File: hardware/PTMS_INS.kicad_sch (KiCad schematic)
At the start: 0 parts

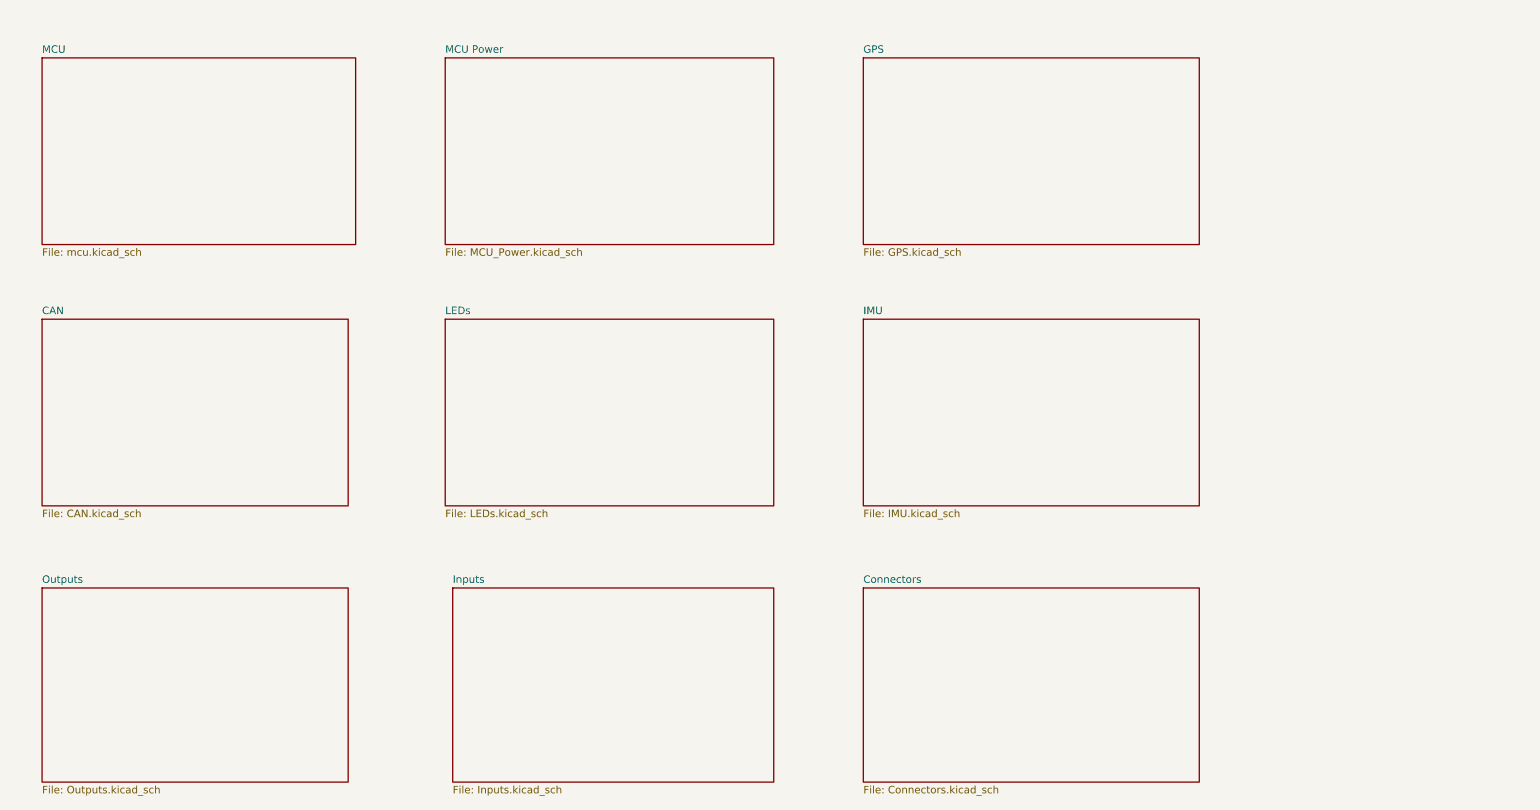
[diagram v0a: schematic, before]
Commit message: wire up altimeter, temp, barometer, imu, gps to MCU
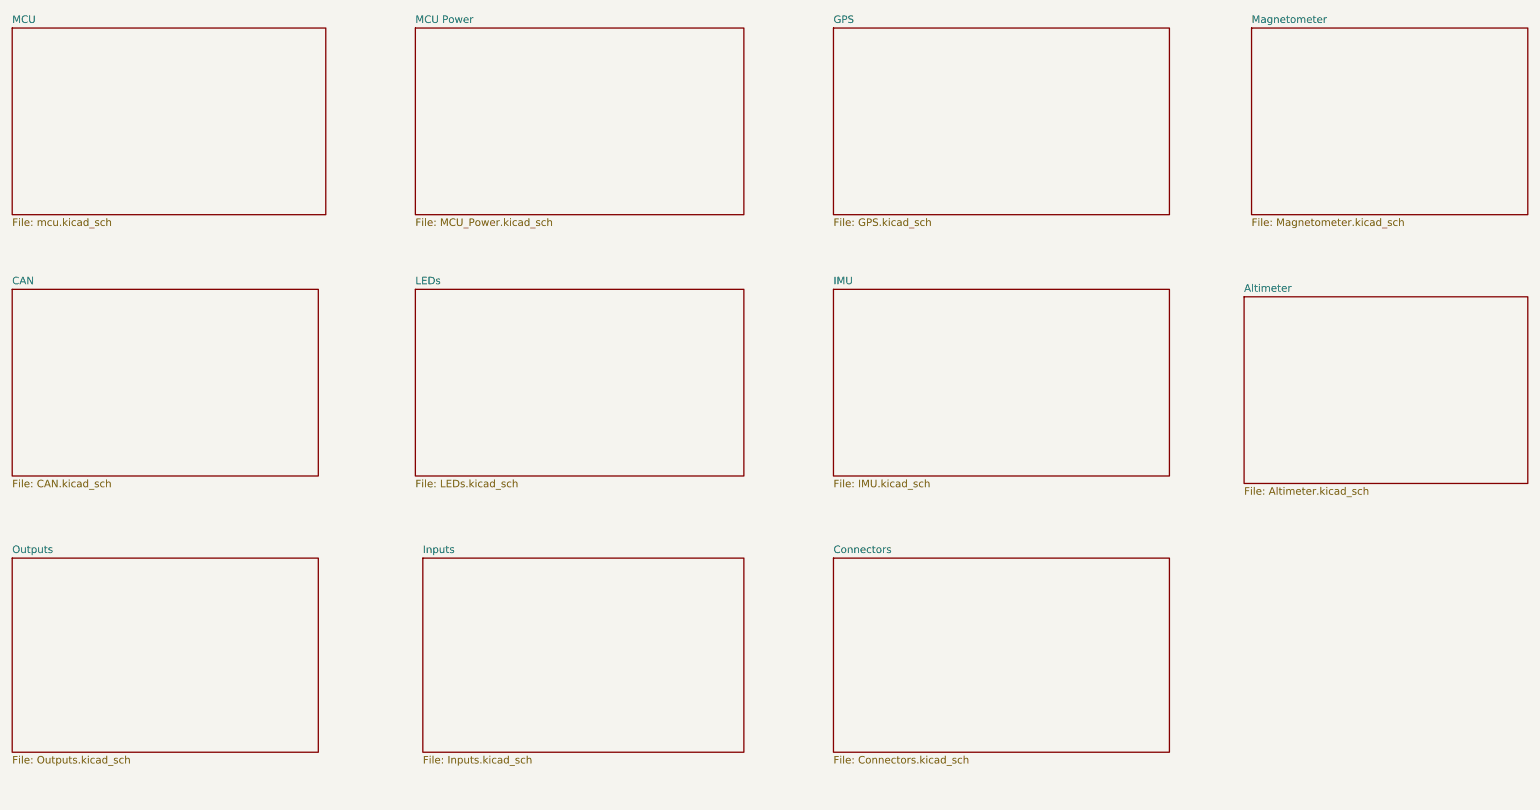
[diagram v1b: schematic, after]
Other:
- added sheet Altimeter (Altimeter.kicad_sch)
- added sheet Magnetometer (Magnetometer.kicad_sch)
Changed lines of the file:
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@@
 	(paper "A4")
 	(sheet
-		(at 25.4 123.19)
+		(at 20.32 118.11)
 		(size 52.07 33.02)
 		(exclude_from_sim no)
@@
 		)
 		(property "Sheetname" "Outputs"
-			(at 25.4 122.4784 0)
+			(at 20.32 117.3984 0)
 			(show_name no)
 			(do_not_autoplace no)
@@
 		)
 		(property "Sheetfile" "Outputs.kicad_sch"
-			(at 25.4 156.7946 0)
+			(at 20.32 151.7146 0)
 			(show_name no)
 			(do_not_autoplace no)
@@
 	)
 	(sheet
-		(at 165.1 77.47)
+		(at 160.02 72.39)
 		(size 57.15 31.75)
 		(exclude_from_sim no)
@@
 		)
 		(property "Sheetname" "IMU"
-			(at 165.1 76.7584 0)
+			(at 160.02 71.6784 0)
 			(show_name no)
 			(do_not_autoplace no)
@@
 		)
 		(property "Sheetfile" "IMU.kicad_sch"
-			(at 165.1 109.8046 0)
+			(at 160.02 104.7246 0)
 			(show_name no)
 			(do_not_autoplace no)
@@
 	)
 	(sheet
-		(at 95.25 123.19)
+		(at 90.17 118.11)
 		(size 54.61 33.02)
 		(exclude_from_sim no)
@@
 		)
 		(property "Sheetname" "Inputs"
-			(at 95.25 122.4784 0)
+			(at 90.17 117.3984 0)
 			(show_name no)
 			(do_not_autoplace no)
@@
 		)
 		(property "Sheetfile" "Inputs.kicad_sch"
-			(at 95.25 156.7946 0)
+			(at 90.17 151.7146 0)
 			(show_name no)
 			(do_not_autoplace no)
@@
 	)
 	(sheet
-		(at 93.98 77.47)
+		(at 229.87 73.66)
+		(size 48.26 31.75)
+		(exclude_from_sim no)
+		(in_bom yes)
+		(on_board yes)
+		(dnp no)
+		(fields_autoplaced yes)
+		(stroke
+			(width 0.1524)
+			(type solid)
+		)
+		(fill
+			(color 0 0 0 0)
+		)
+		(property "Sheetname" "Altimeter"
+			(at 229.87 72.9484 0)
+			(show_name no)
+			(do_not_autoplace no)
+			(effects
+				(font
+					(size 1.27 1.27)
+				)
+				(justify left bottom)
+			)
+		)
+		(property "Sheetfile" "Altimeter.kicad_sch"
+			(at 229.87 105.9946 0)
+			(show_name no)
+			(do_not_autoplace no)
+			(effects
+				(font
+					(size 1.27 1.27)
+				)
+				(justify left top)
+			)
+		)
+		(instances
+			(project "PTMS_INS"
+				(path "/7abec38e-2a6a-4c7d-a187-5990bacce22b"
+					(page "12")
+				)
+			)
+		)
+	)
+	(sheet
+		(at 88.9 72.39)
 		(size 55.88 31.75)
 		(exclude_from_sim no)
@@
 		)
 		(property "Sheetname" "LEDs"
-			(at 93.98 76.7584 0)
+			(at 88.9 71.6784 0)
 			(show_name no)
 			(do_not_autoplace no)
@@
 		)
 		(property "Sheetfile" "LEDs.kicad_sch"
-			(at 93.98 109.8046 0)
+			(at 88.9 104.7246 0)
 			(show_name no)
 			(do_not_autoplace no)
@@
 	)
 	(sheet
-		(at 25.4 33.02)
+		(at 20.32 27.94)
 		(size 53.34 31.75)
 		(exclude_from_sim no)
@@
 		)
 		(property "Sheetname" "MCU"
-			(at 25.4 32.3084 0)
+			(at 20.32 27.2284 0)
 			(show_name no)
 			(do_not_autoplace no)
@@
 		)
 		(property "Sheetfile" "mcu.kicad_sch"
-			(at 25.4 65.3546 0)
+			(at 20.32 60.2746 0)
 			(show_name no)
 			(do_not_autoplace no)
@@
 	)
 	(sheet
-		(at 165.1 123.19)
+		(at 160.02 118.11)
 		(size 57.15 33.02)
 		(exclude_from_sim no)
@@
 		)
 		(property "Sheetname" "Connectors"
-			(at 165.1 122.4784 0)
+			(at 160.02 117.3984 0)
 			(show_name no)
 			(do_not_autoplace no)
@@
 		)
 		(property "Sheetfile" "Connectors.kicad_sch"
-			(at 165.1 156.7946 0)
+			(at 160.02 151.7146 0)
 			(show_name no)
 			(do_not_autoplace no)
@@
 	)
 	(sheet
-		(at 93.98 33.02)
+		(at 231.14 27.94)
+		(size 46.99 31.75)
+		(exclude_from_sim no)
+		(in_bom yes)
+		(on_board yes)
+		(dnp no)
+		(fields_autoplaced yes)
+		(stroke
+			(width 0.1524)
+			(type solid)
+		)
+		(fill
+			(color 0 0 0 0)
+		)
+		(property "Sheetname" "Magnetometer"
+			(at 231.14 27.2284 0)
+			(show_name no)
+			(do_not_autoplace no)
+			(effects
+				(font
+					(size 1.27 1.27)
+				)
+				(justify left bottom)
+			)
+		)
+		(property "Sheetfile" "Magnetometer.kicad_sch"
+			(at 231.14 60.2746 0)
+			(show_name no)
+			(do_not_autoplace no)
+			(effects
+				(font
+					(size 1.27 1.27)
+				)
+				(justify left top)
+			)
+		)
+		(property "Field2" ""
+			(at 231.14 27.94 0)
+			(hide yes)
+			(show_name no)
+			(do_not_autoplace no)
+			(effects
+				(font
+					(size 1.27 1.27)
+				)
+			)
+		)
+		(instances
+			(project "PTMS_INS"
+				(path "/7abec38e-2a6a-4c7d-a187-5990bacce22b"
+					(page "11")
+				)
+			)
+		)
+	)
+	(sheet
+		(at 88.9 27.94)
 		(size 55.88 31.75)
 		(exclude_from_sim no)
@@
 		)
 		(property "Sheetname" "MCU Power"
-			(at 93.98 32.3084 0)
+			(at 88.9 27.2284 0)
 			(show_name no)
 			(do_not_autoplace no)
@@
 		)
 		(property "Sheetfile" "MCU_Power.kicad_sch"
-			(at 93.98 65.3546 0)
+			(at 88.9 60.2746 0)
 			(show_name no)
 			(do_not_autoplace no)
@@
 	)
 	(sheet
-		(at 25.4 77.47)
+		(at 20.32 72.39)
 		(size 52.07 31.75)
 		(exclude_from_sim no)
@@
 		)
 		(property "Sheetname" "CAN"
-			(at 25.4 76.7584 0)
+			(at 20.32 71.6784 0)
 			(show_name no)
 			(do_not_autoplace no)
@@
 		)
 		(property "Sheetfile" "CAN.kicad_sch"
-			(at 25.4 109.8046 0)
+			(at 20.32 104.7246 0)
 			(show_name no)
 			(do_not_autoplace no)
@@
 	)
 	(sheet
-		(at 165.1 33.02)
+		(at 160.02 27.94)
 		(size 57.15 31.75)
 		(exclude_from_sim no)
@@
 		)
 		(property "Sheetname" "GPS"
-			(at 165.1 32.3084 0)
+			(at 160.02 27.2284 0)
 			(show_name no)
 			(do_not_autoplace no)
@@
 		)
 		(property "Sheetfile" "GPS.kicad_sch"
-			(at 165.1 65.3546 0)
-			(show_name no)
-			(do_not_autoplace no)
+			(at 160.02 60.2746 0)
+			(show_name no)
+			(do_not_autoplace no)
